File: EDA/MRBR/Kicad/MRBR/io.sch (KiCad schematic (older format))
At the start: 0 parts

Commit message: Resume schematics conception
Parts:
- added D4: LED, symbol Device:LED
- added R9: 220R, symbol Device:R
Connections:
- new net: D4.2 (A), R9.1
- new net BT_LED: R9.2
- new net GND: D4.1 (K)
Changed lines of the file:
@@
 $Descr A4 11693 8268
 encoding utf-8
-Sheet 1 4
+Sheet 3 4
 Title ""
 Date ""
@@
 Comment4 ""
 $EndDescr
+Text HLabel 4000 1100 0    50   Input ~ 0
+GPIOs
+Text HLabel 4000 1200 0    50   Input ~ 0
+I2C
+Text HLabel 4000 1300 0    50   Input ~ 0
+UART1
+Text HLabel 4000 1400 0    50   Input ~ 0
+UART2
+Wire Bus Line
+	4000 1100 6000 1100
+Entry Wire Line
+	6000 1100 6100 1200
+Entry Wire Line
+	6000 1200 6100 1300
+Entry Wire Line
+	6000 1300 6100 1400
+Entry Wire Line
+	6000 1400 6100 1500
+Entry Wire Line
+	6000 1500 6100 1600
+Entry Wire Line
+	6000 1700 6100 1800
+Entry Wire Line
+	6000 1600 6100 1700
+Text Label 6200 1200 0    50   ~ 0
+BT_LED
+$Comp
+L Device:LED D4
+U 1 1 611CD8F5
+P 7300 1200
+F 0 "D4" H 7293 945 50  0000 C CNN
+F 1 "LED" H 7293 1036 50  0000 C CNN
+F 2 "" H 7300 1200 50  0001 C CNN
+F 3 "~" H 7300 1200 50  0001 C CNN
+	1    7300 1200
+	-1   0    0    1
+$EndComp
+$Comp
+L Device:R R9
+U 1 1 611CECE2
+P 6850 1200
+F 0 "R9" V 6643 1200 50  0000 C CNN
+F 1 "220R" V 6734 1200 50  0000 C CNN
+F 2 "" V 6780 1200 50  0001 C CNN
+F 3 "~" H 6850 1200 50  0001 C CNN
+	1    6850 1200
+	0    1    1    0
+$EndComp
+$Comp
+L power:GND #PWR022
+U 1 1 611CF611
+P 8050 1200
+F 0 "#PWR022" H 8050 950 50  0001 C CNN
+F 1 "GND" H 8055 1027 50  0000 C CNN
+F 2 "" H 8050 1200 50  0001 C CNN
+F 3 "" H 8050 1200 50  0001 C CNN
+	1    8050 1200
+	1    0    0    -1
+$EndComp
+Wire Wire Line
+	6100 1200 6700 1200
+Wire Wire Line
+	7000 1200 7150 1200
+Wire Wire Line
+	7450 1200 8050 1200
+Wire Bus Line
+	6000 1100 6000 2150
 $EndSCHEMATC

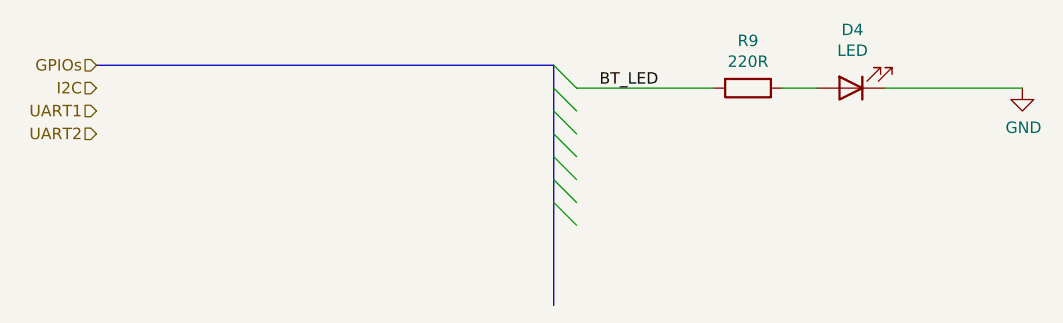
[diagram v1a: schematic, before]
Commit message: Added barrel jack to PSU
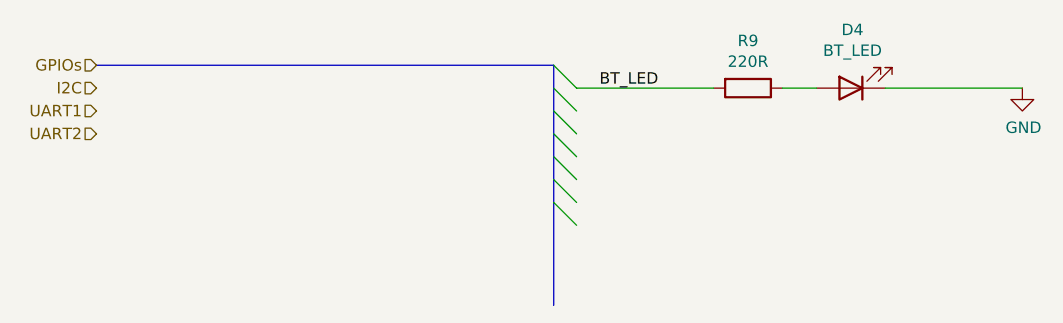
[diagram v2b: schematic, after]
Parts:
- D4: value LED -> BT_LED; footprint (none) -> LED_SMD:LED_1206_3216Metric
- R9: footprint (none) -> Resistor_SMD:R_1206_3216Metric
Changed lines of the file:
@@
 P 7300 1200
 F 0 "D4" H 7293 945 50  0000 C CNN
-F 1 "LED" H 7293 1036 50  0000 C CNN
-F 2 "" H 7300 1200 50  0001 C CNN
+F 1 "BT_LED" H 7293 1036 50  0000 C CNN
+F 2 "LED_SMD:LED_1206_3216Metric" H 7300 1200 50  0001 C CNN
 F 3 "~" H 7300 1200 50  0001 C CNN
 	1    7300 1200
@@
 F 0 "R9" V 6643 1200 50  0000 C CNN
 F 1 "220R" V 6734 1200 50  0000 C CNN
-F 2 "" V 6780 1200 50  0001 C CNN
+F 2 "Resistor_SMD:R_1206_3216Metric" V 6780 1200 50  0001 C CNN
 F 3 "~" H 6850 1200 50  0001 C CNN
 	1    6850 1200
